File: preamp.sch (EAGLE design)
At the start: 70 parts, among them IC1 INA217DW, IC2 OPA134U, IC3 PCM1808, IC4 12.288MHz, IC5 REG1117

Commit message: after review: named wires, add divider to ref voltage, add GND to digital pins
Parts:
- removed J7: (no value), con-amp:MTA04-100
- added J10: (no value), con-amp:MTA05-100
- added R13: 0, rcl:R-EU_R0805
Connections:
- new net N$28: J1.3, R13.2
- net GND: now also J10.1
- net N$15: now also R13.1; no longer J1.3
- net N$18: now also J10.2; no longer J7.1
- net N$19: now also J10.4; no longer J7.3
- net N$8: now also J10.3; no longer J7.2
- net N$9: now also J10.5; no longer J7.4
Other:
- note added: "5V"
- note added: "BCK"
- note added: "DOUT"
- note added: "GND"
- note added: "INL"
- note added: "INR"
- note added: "LRCK"
- note added: "OUT"
- note added: "REF"
- note added: "SCKI"
- note added: "V+"
- note added: "V-"
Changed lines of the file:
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@@
 <part name="IC4" library="rpiadc" deviceset="KXO-97" device="" value="12.288MHz"/>
 <part name="C18" library="rcl" deviceset="C-EU" device="C0805" value="0.1"/>
-<part name="J7" library="con-amp" deviceset="MTA04-100" device=""/>
 <part name="C19" library="rcl" deviceset="C-EU" device="C0805" value="0.1"/>
 <part name="R12" library="rcl" deviceset="R-EU_" device="R0805" value="1k"/>
@@
 <part name="C31" library="rcl" deviceset="CPOL-EU" device="153CLV-0605" value="47"/>
 <part name="R17" library="rcl" deviceset="R-EU_" device="R0805" value="0"/>
+<part name="R13" library="rcl" deviceset="R-EU_" device="R0805" value="0"/>
+<part name="J10" library="con-amp" deviceset="MTA05-100" device=""/>
+<part name="GND6" library="supply1" deviceset="GND" device=""/>
 </parts>
 <sheets>
@@
 4) резистор отвечающий за усиление, оставить ему место на разводке чтобы можно было подбирать
 5) усилители сделать с возможностью отеделения, блок питания так же</text>
+<text x="-30.48" y="81.28" size="1.778" layer="91">GND</text>
+<text x="-30.48" y="83.82" size="1.778" layer="91">INL</text>
+<text x="-30.48" y="78.74" size="1.778" layer="91">INR</text>
+<text x="160.02" y="78.74" size="1.778" layer="91">GND</text>
+<text x="160.02" y="81.28" size="1.778" layer="91">OUT</text>
+<text x="160.02" y="76.2" size="1.778" layer="91">REF</text>
+<text x="116.84" y="116.84" size="1.778" layer="91">GND</text>
+<text x="116.84" y="119.38" size="1.778" layer="91">V+</text>
+<text x="116.84" y="119.38" size="1.778" layer="91">V+</text>
+<text x="116.84" y="114.3" size="1.778" layer="91">V-</text>
+<text x="215.9" y="160.02" size="1.778" layer="91">GND</text>
+<text x="215.9" y="162.56" size="1.778" layer="91">5V</text>
+<text x="213.36" y="96.52" size="1.778" layer="91">REF</text>
+<text x="213.36" y="93.98" size="1.778" layer="91">GND</text>
+<text x="213.36" y="99.06" size="1.778" layer="91">INL</text>
+<text x="213.36" y="101.6" size="1.778" layer="91">INR</text>
+<text x="350.52" y="99.06" size="1.778" layer="91">SCKI</text>
+<text x="350.52" y="101.6" size="1.778" layer="91">LRCK</text>
+<text x="350.52" y="96.52" size="1.778" layer="91">BCK</text>
+<text x="350.52" y="93.98" size="1.778" layer="91">DOUT</text>
+<text x="350.52" y="104.14" size="1.778" layer="91">GND</text>
+<text x="124.46" y="195.58" size="1.778" layer="91">GND</text>
+<text x="124.46" y="198.12" size="1.778" layer="91">V+</text>
+<text x="124.46" y="193.04" size="1.778" layer="91">V-</text>
+<text x="-30.48" y="195.58" size="1.778" layer="91">GND</text>
+<text x="-30.48" y="198.12" size="1.778" layer="91">5V</text>
 </plain>
 <instances>
@@
 <instance part="IC4" gate="G$1" x="307.34" y="132.08"/>
 <instance part="C18" gate="G$1" x="284.48" y="132.08"/>
-<instance part="J7" gate="G$1" x="347.98" y="99.06" rot="R270"/>
 <instance part="C19" gate="G$1" x="147.32" y="33.02" rot="R180"/>
 <instance part="R12" gate="G$1" x="269.24" y="25.4" rot="R90"/>
@@
 <instance part="C31" gate="G$1" x="368.3" y="78.74"/>
 <instance part="R17" gate="G$1" x="370.84" y="63.5" rot="R180"/>
+<instance part="R13" gate="G$1" x="152.4" y="53.34" rot="R90"/>
+<instance part="J10" gate="G$1" x="347.98" y="99.06" rot="R270"/>
+<instance part="GND6" gate="1" x="337.82" y="109.22"/>
 </instances>
 <busses>
@@
 <segment>
 <pinref part="R2" gate="G$1" pin="1"/>
-<wire x1="22.86" y1="86.36" x2="-10.16" y2="86.36" width="0.1524" layer="91"/>
+<wire x1="22.86" y1="86.36" x2="-15.24" y2="86.36" width="0.1524" layer="91"/>
 <wire x1="22.86" y1="93.98" x2="22.86" y2="86.36" width="0.1524" layer="91"/>
 <pinref part="C4" gate="G$1" pin="+"/>
 <wire x1="30.48" y1="86.36" x2="22.86" y2="86.36" width="0.1524" layer="91"/>
 <junction x="22.86" y="86.36"/>
-<wire x1="-10.16" y1="83.82" x2="-10.16" y2="86.36" width="0.1524" layer="91"/>
 <pinref part="J2" gate="G$1" pin="1"/>
 <wire x1="-20.32" y1="78.74" x2="-15.24" y2="78.74" width="0.1524" layer="91"/>
-<wire x1="-15.24" y1="78.74" x2="-15.24" y2="83.82" width="0.1524" layer="91"/>
-<wire x1="-15.24" y1="83.82" x2="-10.16" y2="83.82" width="0.1524" layer="91"/>
+<wire x1="-15.24" y1="78.74" x2="-15.24" y2="86.36" width="0.1524" layer="91"/>
 </segment>
 </net>
@@
 <wire x1="15.24" y1="73.66" x2="30.48" y2="73.66" width="0.1524" layer="91"/>
 <junction x="15.24" y="73.66"/>
-<wire x1="-10.16" y1="78.74" x2="-10.16" y2="73.66" width="0.1524" layer="91"/>
-<wire x1="-10.16" y1="78.74" x2="-7.62" y2="78.74" width="0.1524" layer="91"/>
 <pinref part="J2" gate="G$1" pin="3"/>
 <wire x1="-20.32" y1="83.82" x2="-17.78" y2="83.82" width="0.1524" layer="91"/>
 <wire x1="-17.78" y1="83.82" x2="-17.78" y2="88.9" width="0.1524" layer="91"/>
-<wire x1="-17.78" y1="88.9" x2="-7.62" y2="88.9" width="0.1524" layer="91"/>
-<wire x1="-7.62" y1="88.9" x2="-7.62" y2="78.74" width="0.1524" layer="91"/>
+<wire x1="-17.78" y1="88.9" x2="-10.16" y2="88.9" width="0.1524" layer="91"/>
+<wire x1="-10.16" y1="88.9" x2="-10.16" y2="73.66" width="0.1524" layer="91"/>
 </segment>
 </net>
@@
 <wire x1="147.32" y1="43.18" x2="147.32" y2="38.1" width="0.1524" layer="91"/>
 <junction x="139.7" y="43.18"/>
-<wire x1="152.4" y1="76.2" x2="152.4" y2="43.18" width="0.1524" layer="91"/>
 <wire x1="152.4" y1="43.18" x2="147.32" y2="43.18" width="0.1524" layer="91"/>
 <junction x="147.32" y="43.18"/>
-<pinref part="J1" gate="G$1" pin="3"/>
-<wire x1="154.94" y1="76.2" x2="152.4" y2="76.2" width="0.1524" layer="91"/>
+<pinref part="R13" gate="G$1" pin="1"/>
+<wire x1="152.4" y1="43.18" x2="152.4" y2="48.26" width="0.1524" layer="91"/>
 </segment>
 </net>
@@
 <wire x1="332.74" y1="104.14" x2="332.74" y2="132.08" width="0.1524" layer="91"/>
 <wire x1="332.74" y1="132.08" x2="320.04" y2="132.08" width="0.1524" layer="91"/>
-<wire x1="342.9" y1="104.14" x2="332.74" y2="104.14" width="0.1524" layer="91"/>
+<wire x1="340.36" y1="104.14" x2="332.74" y2="104.14" width="0.1524" layer="91"/>
 <junction x="332.74" y="104.14"/>
-<wire x1="342.9" y1="104.14" x2="342.9" y2="99.06" width="0.1524" layer="91"/>
-<pinref part="J7" gate="G$1" pin="2"/>
-<wire x1="342.9" y1="99.06" x2="345.44" y2="99.06" width="0.1524" layer="91"/>
+<wire x1="340.36" y1="104.14" x2="340.36" y2="99.06" width="0.1524" layer="91"/>
+<wire x1="340.36" y1="99.06" x2="345.44" y2="99.06" width="0.1524" layer="91"/>
+<pinref part="J10" gate="G$1" pin="3"/>
 </segment>
 </net>
@@
 <wire x1="335.28" y1="101.6" x2="335.28" y2="91.44" width="0.1524" layer="91"/>
 <wire x1="335.28" y1="91.44" x2="342.9" y2="91.44" width="0.1524" layer="91"/>
-<pinref part="J7" gate="G$1" pin="4"/>
 <wire x1="345.44" y1="93.98" x2="342.9" y2="93.98" width="0.1524" layer="91"/>
 <wire x1="342.9" y1="91.44" x2="342.9" y2="93.98" width="0.1524" layer="91"/>
+<pinref part="J10" gate="G$1" pin="5"/>
 </segment>
 </net>
@@
 <wire x1="360.68" y1="63.5" x2="365.76" y2="63.5" width="0.1524" layer="91"/>
 <junction x="360.68" y="63.5"/>
+</segment>
+<segment>
+<pinref part="GND6" gate="1" pin="GND"/>
+<wire x1="337.82" y1="111.76" x2="337.82" y2="114.3" width="0.1524" layer="91"/>
+<wire x1="337.82" y1="114.3" x2="342.9" y2="114.3" width="0.1524" layer="91"/>
+<wire x1="342.9" y1="114.3" x2="342.9" y2="104.14" width="0.1524" layer="91"/>
+<pinref part="J10" gate="G$1" pin="1"/>
+<wire x1="342.9" y1="104.14" x2="345.44" y2="104.14" width="0.1524" layer="91"/>
 </segment>
 </net>
@@
 <net name="N$18" class="0">
 <segment>
-<pinref part="J7" gate="G$1" pin="1"/>
 <wire x1="345.44" y1="101.6" x2="337.82" y2="101.6" width="0.1524" layer="91"/>
 <wire x1="337.82" y1="101.6" x2="337.82" y2="96.52" width="0.1524" layer="91"/>
 <pinref part="IC3" gate="G$1" pin="LRCK"/>
 <wire x1="337.82" y1="96.52" x2="327.66" y2="96.52" width="0.1524" layer="91"/>
+<pinref part="J10" gate="G$1" pin="2"/>
 </segment>
 </net>
@@
 <wire x1="327.66" y1="93.98" x2="340.36" y2="93.98" width="0.1524" layer="91"/>
 <wire x1="340.36" y1="93.98" x2="340.36" y2="96.52" width="0.1524" layer="91"/>
-<pinref part="J7" gate="G$1" pin="3"/>
 <wire x1="340.36" y1="96.52" x2="345.44" y2="96.52" width="0.1524" layer="91"/>
+<pinref part="J10" gate="G$1" pin="4"/>
 </segment>
 </net>
@@
 </segment>
 </net>
+<net name="N$28" class="0">
+<segment>
+<pinref part="J1" gate="G$1" pin="3"/>
+<wire x1="154.94" y1="76.2" x2="152.4" y2="76.2" width="0.1524" layer="91"/>
+<pinref part="R13" gate="G$1" pin="2"/>
+<wire x1="152.4" y1="58.42" x2="152.4" y2="76.2" width="0.1524" layer="91"/>
+</segment>
+</net>

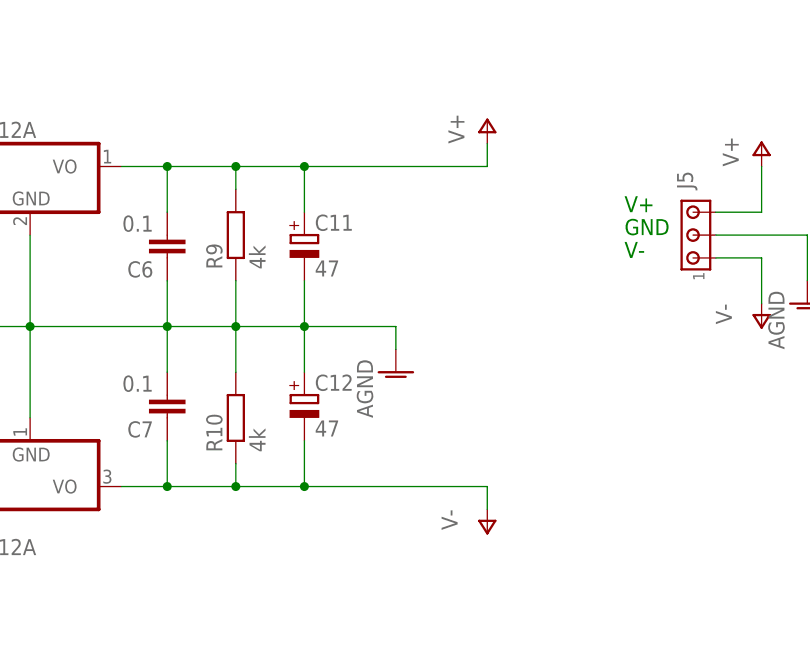
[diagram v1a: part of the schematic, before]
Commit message: fix preamp dimentions, route power supply
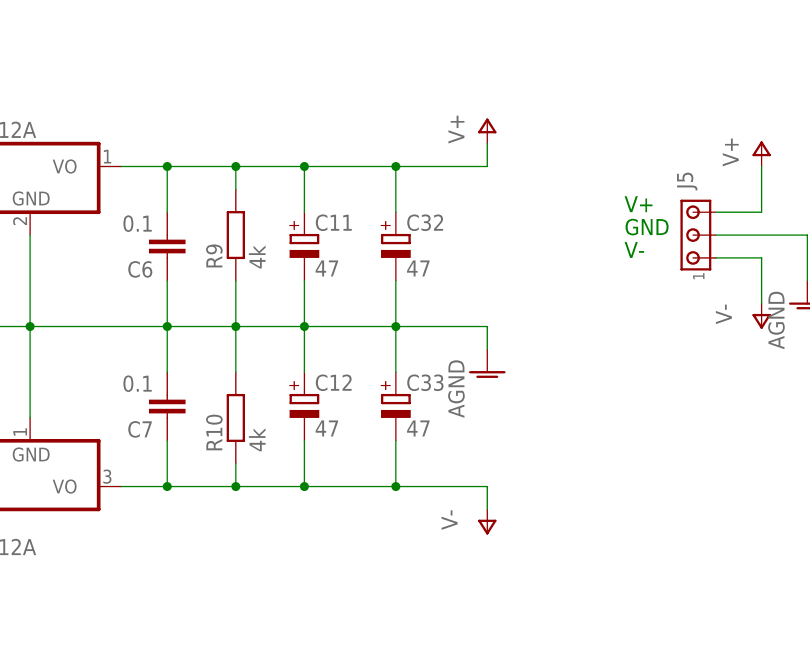
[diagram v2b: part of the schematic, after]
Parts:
- added C32, C33: 47, rcl:CPOL-EU153CLV-0605
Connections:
- net AGND: now also C32.-, C33.+
- net V+: now also C32.+
- net V-: now also C33.-
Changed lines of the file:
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@@
 <part name="J10" library="con-amp" deviceset="MTA05-100" device=""/>
 <part name="GND6" library="supply1" deviceset="GND" device=""/>
+<part name="C32" library="rcl" deviceset="CPOL-EU" device="153CLV-0605" value="47"/>
+<part name="C33" library="rcl" deviceset="CPOL-EU" device="153CLV-0605" value="47"/>
 </parts>
 <sheets>
@@
 <instance part="P+3" gate="1" x="109.22" y="208.28"/>
 <instance part="P-6" gate="1" x="109.22" y="162.56"/>
-<instance part="AGND11" gate="VR1" x="99.06" y="180.34"/>
+<instance part="AGND11" gate="VR1" x="109.22" y="180.34"/>
 <instance part="J6" gate="G$1" x="-22.86" y="195.58" rot="R90"/>
 <instance part="C6" gate="G$1" x="73.66" y="193.04" rot="R180"/>
@@
 <instance part="J10" gate="G$1" x="347.98" y="99.06" rot="R270"/>
 <instance part="GND6" gate="1" x="337.82" y="109.22"/>
+<instance part="C32" gate="G$1" x="99.06" y="195.58"/>
+<instance part="C33" gate="G$1" x="99.06" y="177.8"/>
 </instances>
 <busses>
@@
 <segment>
 <pinref part="AGND11" gate="VR1" pin="AGND"/>
-<wire x1="99.06" y1="182.88" x2="99.06" y2="185.42" width="0.1524" layer="91"/>
+<wire x1="109.22" y1="182.88" x2="109.22" y2="185.42" width="0.1524" layer="91"/>
 <pinref part="R10" gate="G$1" pin="2"/>
 <pinref part="R9" gate="G$1" pin="1"/>
 <wire x1="81.28" y1="180.34" x2="81.28" y2="185.42" width="0.1524" layer="91"/>
 <wire x1="81.28" y1="185.42" x2="81.28" y2="190.5" width="0.1524" layer="91"/>
-<wire x1="99.06" y1="185.42" x2="88.9" y2="185.42" width="0.1524" layer="91"/>
+<wire x1="109.22" y1="185.42" x2="99.06" y2="185.42" width="0.1524" layer="91"/>
 <pinref part="U$3" gate="IC$1" pin="GND"/>
 <pinref part="U$2" gate="G$1" pin="GND"/>
+<wire x1="99.06" y1="185.42" x2="88.9" y2="185.42" width="0.1524" layer="91"/>
 <wire x1="88.9" y1="185.42" x2="81.28" y2="185.42" width="0.1524" layer="91"/>
 <wire x1="58.42" y1="195.58" x2="58.42" y2="185.42" width="0.1524" layer="91"/>
@@
 <junction x="73.66" y="185.42"/>
 <junction x="88.9" y="185.42"/>
+<pinref part="C32" gate="G$1" pin="-"/>
+<wire x1="99.06" y1="190.5" x2="99.06" y2="185.42" width="0.1524" layer="91"/>
+<pinref part="C33" gate="G$1" pin="+"/>
+<wire x1="99.06" y1="180.34" x2="99.06" y2="185.42" width="0.1524" layer="91"/>
+<junction x="99.06" y="185.42"/>
 </segment>
 <segment>
@@
 <junction x="73.66" y="203.2"/>
 <junction x="88.9" y="203.2"/>
-<wire x1="88.9" y1="203.2" x2="109.22" y2="203.2" width="0.1524" layer="91"/>
+<wire x1="88.9" y1="203.2" x2="99.06" y2="203.2" width="0.1524" layer="91"/>
+<pinref part="C32" gate="G$1" pin="+"/>
+<wire x1="99.06" y1="203.2" x2="109.22" y2="203.2" width="0.1524" layer="91"/>
+<wire x1="99.06" y1="198.12" x2="99.06" y2="203.2" width="0.1524" layer="91"/>
+<junction x="99.06" y="203.2"/>
 </segment>
 </net>
@@
 <junction x="73.66" y="167.64"/>
 <junction x="88.9" y="167.64"/>
-<wire x1="88.9" y1="167.64" x2="109.22" y2="167.64" width="0.1524" layer="91"/>
-</segment>
-</net>
+<wire x1="88.9" y1="167.64" x2="99.06" y2="167.64" width="0.1524" layer="91"/>
+<pinref part="C33" gate="G$1" pin="-"/>
+<wire x1="99.06" y1="167.64" x2="109.22" y2="167.64" width="0.1524" layer="91"/>
+<wire x1="99.06" y1="172.72" x2="99.06" y2="167.64" width="0.1524" layer="91"/>
+<junction x="99.06" y="167.64"/>
+</segment>
+</net>
